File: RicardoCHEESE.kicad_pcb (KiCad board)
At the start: 4 copper layers, 138 parts, among them IC1 SiC437BED-T1-GE3, J0 Conn_01x05_Male, J1 Conn_01x05_Male, J10 USB_C_Receptacle_USB2.0, J101 RBUS, J2 Conn_01x05_Male, J3 Conn_01x05_Male, J4 Conn_Coaxial, J601 Conn_01x02_Male, U1 HEF4051BT, U101 ESP32-S3, U201 SN65HVD230, U3 RTC6705, U4 SE5005L, U401 LM66200DRLR, U402 MAX77827AEFD+T, U403 SC4215, Y101 40MHz±10ppm, Y3 8MHz

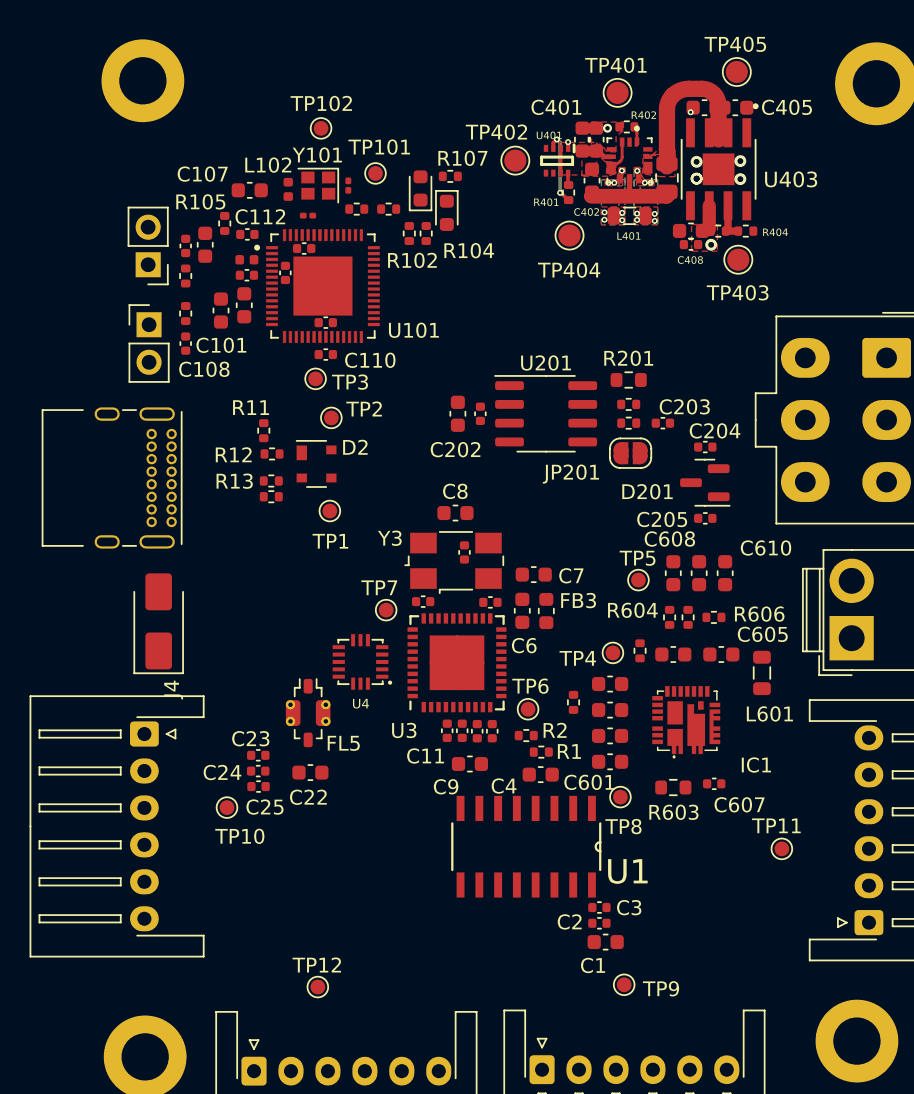
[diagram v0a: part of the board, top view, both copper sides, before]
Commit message: Add photo triggers
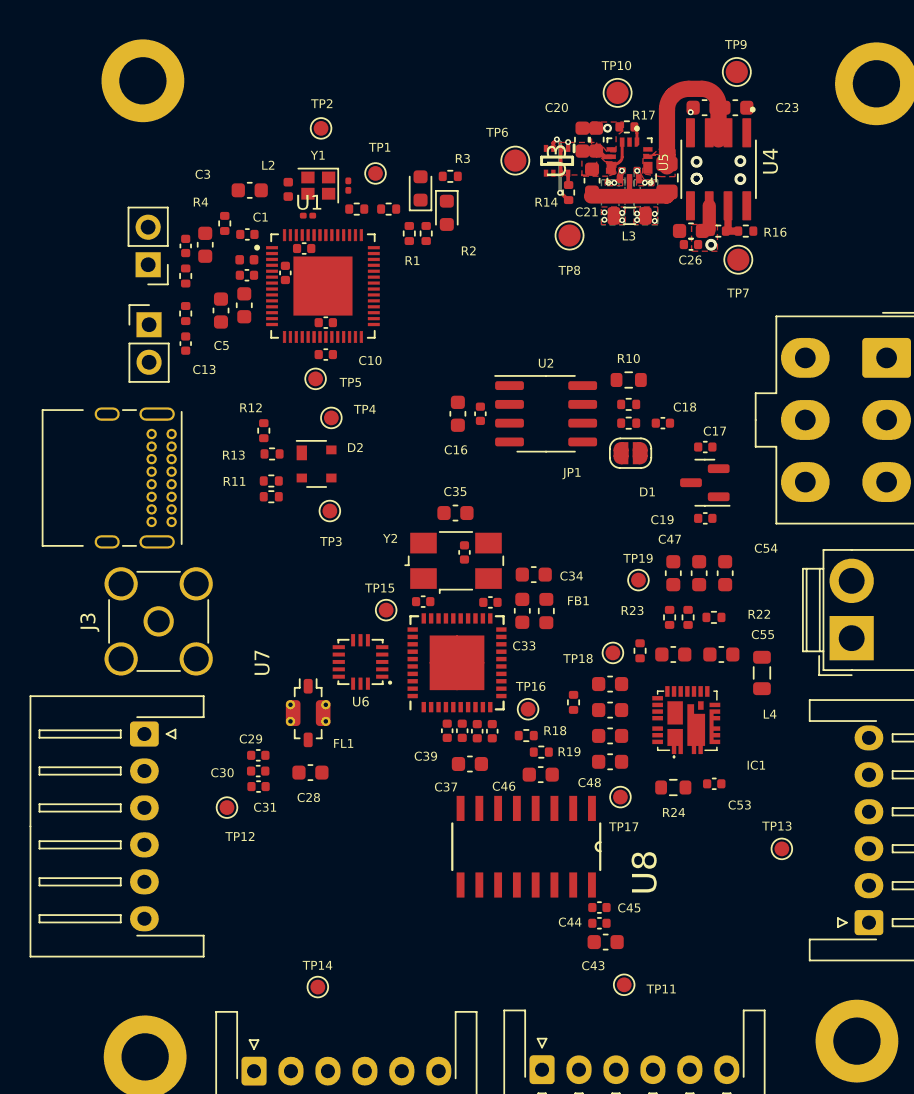
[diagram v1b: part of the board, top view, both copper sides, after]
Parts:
- J3: renamed from J4; footprint Diode_SMD:D_SMA -> Connector_Coaxial:SMA_Amphenol_901-144_Vertical
- U1: renamed from U101; footprint iclr:QFN40P700X700X90-57N -> fps:QFN40P700X700X90-57N
- U3: renamed from U401; footprint iclr:SOTFL50P160X60-8N -> fps:SOTFL50P160X60-8N
- U4: renamed from U403; footprint iclr:SOIC127P599X175-9N -> fps:SOIC127P599X175-8N
- U5: renamed from U402; footprint iclr:CONV_MAX77827AEFD+T -> fps:CONV_MAX77827AEFD+T
- U6: renamed from U4; footprint iclr:QFN300X300X100-16N -> fps:QFN300X300X100-16N
- U7: renamed from U3; footprint Custom:RTC6705 -> Ricardo-CHEESE:RTC6705
- U8: renamed from U1; footprint HEF4051BT:SOIC127P600X175-16N -> Ricardo-CHEESE:SOIC127P600X175-16N
- renumbered 12VLED101 to 12VLED1, 3V3LED101 to 3V3LED1, BOOTJUMPER101 to BOOTJUMPER1, C112 to C1, C110 to C10, C111 to C11, C103 to C12, C108 to C13, C102 to C14, C201 to C15, C202 to C16, C204 to C17, C203 to C18, C205 to C19, C113 to C2, C401 to C20, C402 to C21, C404 to C22, C405 to C23, C406 to C24, C407 to C25, C408 to C26, C403 to C27, C22 to C28, C23 to C29, C107 to C3, C24 to C30, C25 to C31, C5 to C32, C6 to C33, C7 to C34, C8 to C35, C14 to C36, C9 to C37, C10 to C38, C11 to C39, C109 to C4, C12 to C40, C13 to C41, C15 to C42, C1 to C43, C2 to C44, C3 to C45, C4 to C46, C608 to C47, C601 to C48, C602 to C49, C101 to C5, C603 to C50, C604 to C51, C609 to C52, C607 to C53, C610 to C54, C605 to C55, C606 to C56, C104 to C6, C105 to C7, C106 to C8, C114 to C9, D201 to D1, ENJUMPER101 to ENJUMPER1, FB3 to FB1, FL5 to FL1, H101 to H1, H102 to H2, H103 to H3, H104 to H4, J101 to J1, J10 to J2, J0 to J4, J1 to J5, J2 to J6, J3 to J7, J601 to J8, JP201 to JP1, L101 to L1, L102 to L2, L401 to L3, L601 to L4, R102 to R1, R201 to R10, R13 to R11, R11 to R12, R12 to R13, R401 to R14, R403 to R15, R404 to R16, R402 to R17, R2 to R18, R1 to R19, R104 to R2, R602 to R20, R605 to R21, R606 to R22, R604 to R23, R603 to R24, R601 to R25, R107 to R3, R105 to R4, R106 to R5, R101 to R6, R103 to R7, R202 to R8, R203 to R9, TP101 to TP1, TP401 to TP10, TP9 to TP11, TP10 to TP12, TP11 to TP13, TP12 to TP14, TP7 to TP15, TP6 to TP16, TP8 to TP17, TP4 to TP18, TP5 to TP19, TP102 to TP2, TP1 to TP3, TP2 to TP4, TP3 to TP5, TP402 to TP6, TP403 to TP7, TP404 to TP8, TP405 to TP9, TXLED101 to TXLED1, U201 to U2, Y101 to Y1, Y3 to Y2

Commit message: Fixed libraries and footprints
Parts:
- added R26: 1k, Resistor_SMD:R_0402_1005Metric, F.Cu at (209.7, 91.1)
- added R27: 1k, Resistor_SMD:R_0402_1005Metric, F.Cu at (209.7, 93.1)
- added R28: 1k, Resistor_SMD:R_0402_1005Metric, F.Cu at (209.7, 95.1)
- added R29: 1k, Resistor_SMD:R_0402_1005Metric, F.Cu at (209.7, 97.1)
- added R30: 1k, Resistor_SMD:R_0402_1005Metric, F.Cu at (209.7, 99.1)
- added R31: 1k, Resistor_SMD:R_0402_1005Metric, F.Cu at (212.6, 91.1)
- added R32: 1k, Resistor_SMD:R_0402_1005Metric, F.Cu at (212.6, 93.1)
- added R33: 1k, Resistor_SMD:R_0402_1005Metric, F.Cu at (212.6, 95.1)
- added R34: 1k, Resistor_SMD:R_0402_1005Metric, F.Cu at (212.6, 97.1)
- added R35: 1k, Resistor_SMD:R_0402_1005Metric, F.Cu at (212.6, 99.1)
- IC1: footprint SIC437BED-T1-GE3:SIC437BEDT1GE3 -> fps:SiC437BEDT1GE3
- J3: footprint Connector_Coaxial:SMA_Amphenol_901-144_Vertical -> Connector_Coaxial:SMA_Molex_73251-1153_EdgeMount_Horizontal
- J4, J5, J6, J7: value Conn_01x05_Male -> Conn_01x06_Pin; footprint Connector_JST:JST_XH_S6B-XH-A-1_1x06_P2.50mm_Horizontal -> Connector_JST:JST_PH_S6B-PH-K_1x06_P2.00mm_Horizontal
- moved J4 5.46 mm to (159.8, 127.6)
- moved J5 5.27 mm to (139.5, 112.2)
- moved J3 2.77 mm to (138.3, 102.3), turned to 0 degrees
- moved J7 2.52 mm to (144.3, 127.7)
- moved J6 2.26 mm to (184.8, 119.0)
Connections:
- J4 pad 1: 5V_PWR -> Net-(J4-Pin_1)
- J4 pad 4: CAMERA_PWR_DET -> Net-(J4-Pin_4)
- J4 pad 5: CAMERA0_TRIG -> Net-(J4-Pin_5)
- J4 pad 6: (no net) -> Net-(J4-Pin_6)
- J5 pad 1: 5V_PWR -> Net-(J4-Pin_1)
- J5 pad 4: CAMERA_PWR_DET -> Net-(J4-Pin_4)
- J5 pad 5: CAMERA1_TRIG -> Net-(J5-Pin_5)
- J5 pad 6: (no net) -> Net-(J5-Pin_6)
- J6 pad 1: 5V_PWR -> Net-(J4-Pin_1)
- J6 pad 4: CAMERA_PWR_DET -> Net-(J4-Pin_4)
- J6 pad 5: CAMERA2_TRIG -> Net-(J6-Pin_5)
- J6 pad 6: (no net) -> Net-(J6-Pin_6)
- J7 pad 1: 5V_PWR -> Net-(J4-Pin_1)
- J7 pad 4: CAMERA_PWR_DET -> Net-(J4-Pin_4)
- J7 pad 5: CAMERA3_TRIG -> Net-(J7-Pin_5)
- J7 pad 6: (no net) -> Net-(J7-Pin_6)
- U1 pad 16: CAMERA0_TRIG -> PHOTO0_TRIG
- U1 pad 17: CAMERA1_TRIG -> PHOTO1_TRIG
- U1 pad 18: CAMERA2_TRIG -> PHOTO2_TRIG
- U1 pad 19: CAMERA3_TRIG -> PHOTO3_TRIG
- U1 pad 38: unconnected-(U1-GPIO33-Pad38) -> CAMERA0_TRIG
- U1 pad 39: unconnected-(U1-GPIO34-Pad39) -> CAMERA1_TRIG
- U1 pad 40: unconnected-(U1-GPIO35-Pad40) -> CAMERA2_TRIG
- U1 pad 41: unconnected-(U1-GPIO36-Pad41) -> CAMERA3_TRIG
- U4 pad 5: (no net) -> unconnected-(U4-NC-Pad5)

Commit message: User saved
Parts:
- moved R31 76.4 mm to (142.8, 122.1)
- moved R30 70.2 mm to (142.8, 120.3)
- moved R34 66.2 mm to (152.4, 124.5), turned to 90 degrees
- moved R27 66.0 mm to (144.8, 81.1), turned to 90 degrees
- moved R35 63.5 mm to (154.4, 124.5), turned to 90 degrees
- moved R26 53.1 mm to (166.0, 121.3)
- moved R28 51.2 mm to (167.8, 124.5), turned to -90 degrees
- moved R29 48.4 mm to (169.8, 124.4), turned to 90 degrees
- moved R32 35.9 mm to (181.6, 111.1)
- moved R33 34.0 mm to (181.6, 109.1)
- moved TP11 7.11 mm to (172.0, 117.3)

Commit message: Placing footprints
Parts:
- moved C19 54.4 mm to (212.7, 52.7), turned to 90 degrees
- moved C16 52.3 mm to (208.1, 67.3), turned to 0 degrees
- moved JP1 51.0 mm to (210.3, 56.1), turned to 180 degrees
- moved D1 51.0 mm to (210.3, 52.7), turned to -90 degrees
- moved C15 50.9 mm to (207.5, 66.0), turned to 0 degrees
- moved U2 47.7 mm to (206.3, 61.7), turned to 90 degrees
- moved C17 47.6 mm to (207.9, 52.7), turned to 90 degrees
- moved C18 47.1 mm to (207.9, 54.7), turned to 90 degrees
- moved R9 46.7 mm to (207.0, 56.9), turned to -90 degrees
- moved R8 44.9 mm to (205.7, 56.9), turned to 90 degrees
- moved J1 43.8 mm to (203.9, 41.0), turned to 0 degrees
- moved C21 41.9 mm to (202.9, 93.1)
- moved C24 41.9 mm to (210.6, 88.1)
- moved C27 41.9 mm to (203.2, 90.3)
- moved R16 41.9 mm to (213.3, 96.5)
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
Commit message: Board layout
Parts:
- moved TP7 80.7 mm to (136.2, 73.2), turned to 180 degrees
- moved R16 79.3 mm to (136.9, 75.2), turned to 180 degrees
- moved C23 76.0 mm to (136.8, 84.0), turned to 180 degrees
- moved R15 75.6 mm to (138.9, 75.2), turned to 180 degrees
- moved TP9 74.1 mm to (138.7, 86.4), turned to 180 degrees
- moved U4 73.7 mm to (138.9, 79.4), turned to 90 degrees
- moved C25 72.4 mm to (140.9, 73.8), turned to 180 degrees
- moved C26 72.2 mm to (140.9, 75.2), turned to 180 degrees
- moved C16 72.2 mm to (135.8, 68.4), turned to -90 degrees
- moved C24 70.8 mm to (139.8, 84.0), turned to 0 degrees
- moved C15 70.4 mm to (137.2, 67.8), turned to -90 degrees
- moved C22 66.7 mm to (142.8, 78.9), turned to 90 degrees
- moved C19 65.5 mm to (150.4, 73.0), turned to 0 degrees
- moved U2 65.0 mm to (141.5, 66.6), turned to 0 degrees
- moved JP1 64.9 mm to (147.1, 70.6), turned to 90 degrees
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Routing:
- net /Power/BBOUT: track 12.3 -> 0.00 mm
- net GND: track 6.73 -> 0.00 mm, vias 8 -> 0
- net VBUS: track 5.27 -> 0.00 mm, vias 2 -> 0
- net /Power/FBIn: track 2.61 -> 0.00 mm
- net /Power/BBIN: track 2.00 -> 0.00 mm
- net /Power/VoutDiode: track 1.68 -> 0.00 mm
- net +3.3V: track 1.61 -> 0.00 mm, vias 1 -> 0
- net /Power/BIAS: track 1.42 -> 0.00 mm
- net /Power/SEL: track 1.01 -> 0.00 mm
- net Net-(U3-ST): track 0.81 -> 0.00 mm
- net /Power/LX2: vias 7 -> 0
- net /Power/LX1: vias 7 -> 0
- removed copper zone on F.Cu, net +3.3V
- removed copper zone on F.Cu, net /Power/BBIN
- removed copper zone on F.Cu, net /Power/BBOUT
- removed copper zone on B.Cu, net /Power/LX1
- removed copper zone on F.Cu, net /Power/LX1
- removed copper zone on B.Cu, net /Power/LX2
- removed copper zone on F.Cu, net /Power/LX2
- removed copper zone on F.Cu, net GND
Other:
- board outline added: 54.4 x 77.3 mm

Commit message: Some routing
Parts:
- moved J8 4.42 mm to (162.5, 95.8), turned to -90 degrees
- turned R28 to 90 degrees
- turned R32 to 180 degrees
- turned R33 to 180 degrees
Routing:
- net Net-(J4-Pin_4): track 0.00 -> 69.5 mm
- net /Camera System/CAMERA1: track 0.00 -> 27.1 mm
- net GND: track 0.00 -> 26.0 mm, vias 0 -> 8
- net +3.3V: track 0.00 -> 25.0 mm
- net /Camera System/CAMERA2: track 0.00 -> 21.0 mm
- net /Data+: track 0.00 -> 20.6 mm, vias 0 -> 1
- net /Camera System/CAMERA3: track 0.00 -> 19.1 mm
- net Net-(IC1-VIN_1): track 0.00 -> 18.7 mm
- net /Data-: track 0.00 -> 17.2 mm
- net /CAN+: track 0.00 -> 16.3 mm
- net /CAN-: track 0.00 -> 15.5 mm
- net RBUS_uC_V: track 0.00 -> 13.9 mm
- net Net-(IC1-SW_1): track 0.00 -> 13.3 mm
- net 5V_PWR: track 0.00 -> 12.8 mm
- net +3.3VA: track 0.00 -> 11.9 mm, vias 0 -> 2
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- added copper zone on In2.Cu, net GND

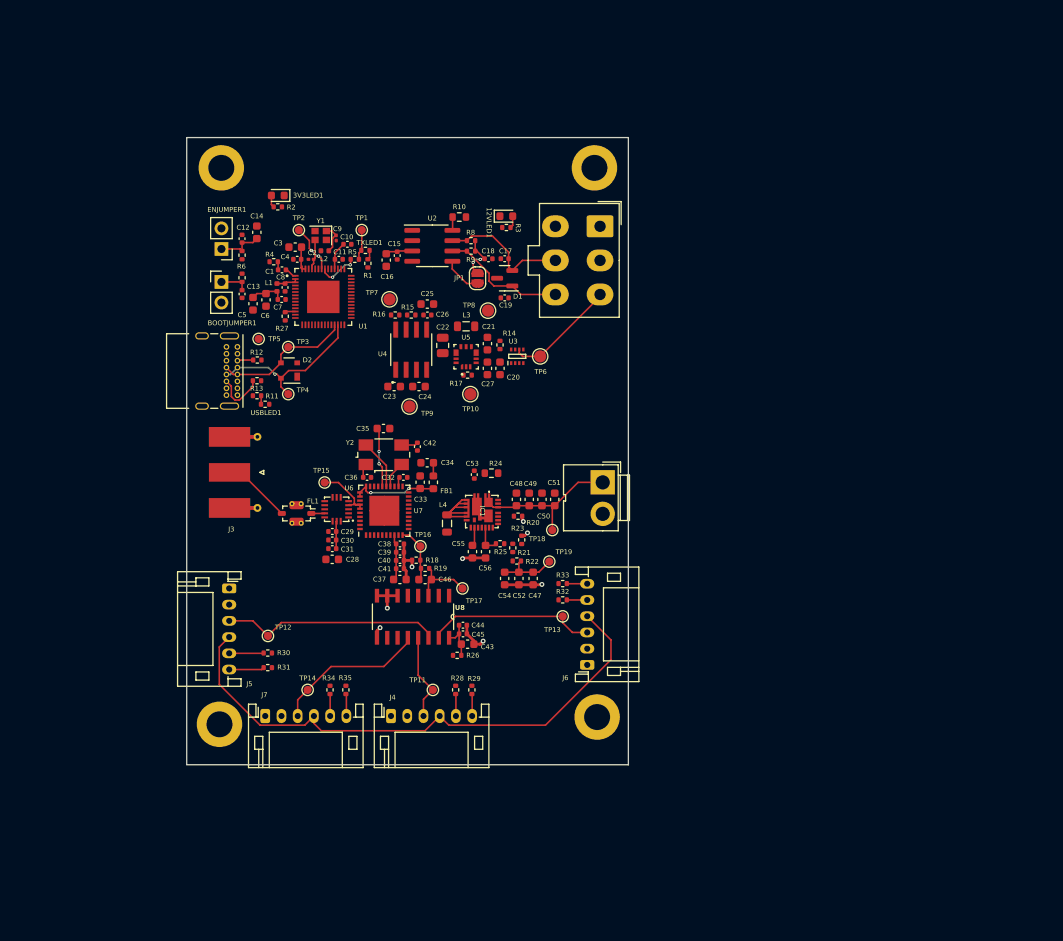
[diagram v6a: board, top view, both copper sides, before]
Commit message: Camera buck changes, c and r footprints, other
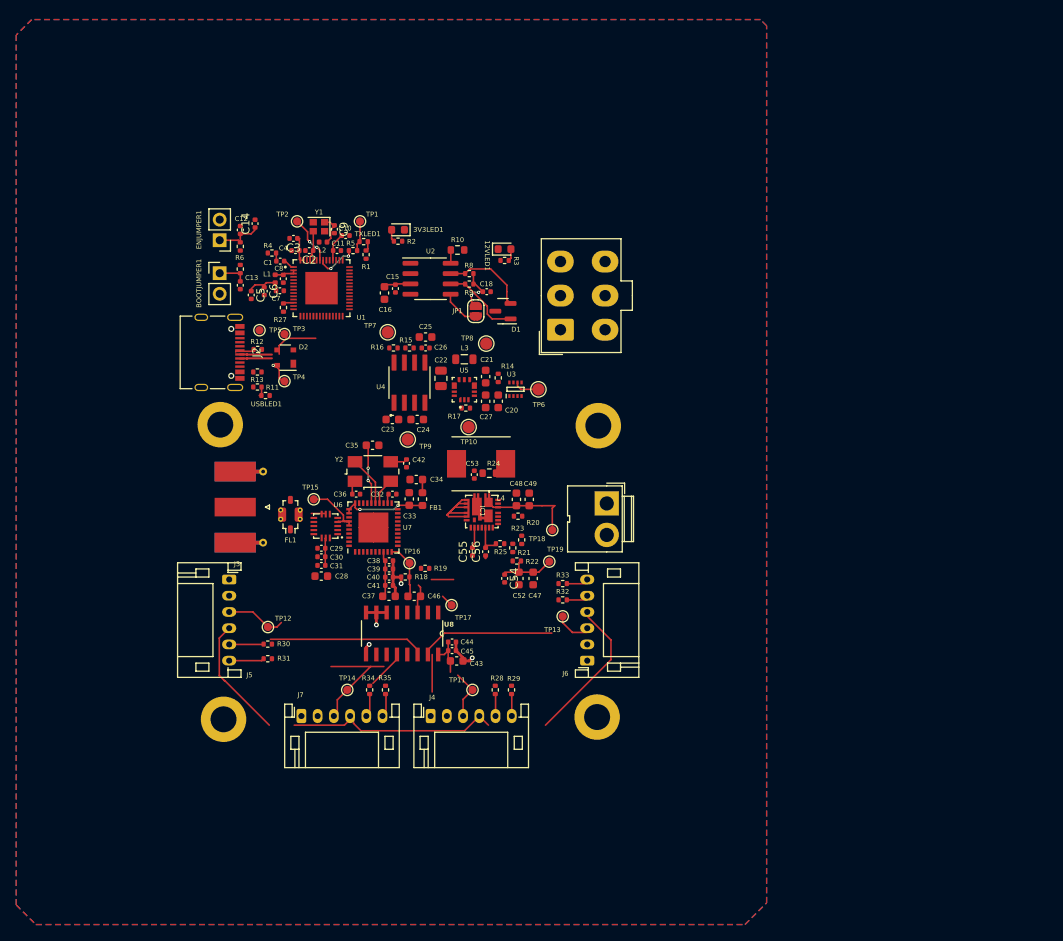
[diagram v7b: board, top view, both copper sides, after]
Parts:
- removed C17, C19: 220pF, Capacitor_SMD:C_0402_1005Metric
- removed C50, C51: 2u2, Capacitor_SMD:C_0603_1608Metric
- removed R26: 1k, Resistor_SMD:R_0402_1005Metric
- C14, C3, C5, C55, C56, C6: footprint Capacitor_SMD:C_0603_1608Metric -> Capacitor_SMD:C_0402_1005Metric
- C2, C9: footprint Capacitor_SMD:C_0201_0603Metric -> Capacitor_SMD:C_0402_1005Metric
- C49: value 2u2 -> 1u5
- C54: value 3u3 -> 100n; footprint Capacitor_SMD:C_0603_1608Metric -> Capacitor_SMD:C_0402_1005Metric
- J2: footprint Connector_USB:USB_C_Receptacle_GCT_USB4085 -> Connector_USB:USB_C_Receptacle_Palconn_UTC16-G
- L4: footprint Inductor_SMD:L_0805_2012Metric -> Ricardo-CHEESE:IND_ASPI-0630HI-6R8M-T15
- R25: value 51k -> 200k
- moved H2 31.8 mm to (161.9, 88.8)
- moved H1 31.6 mm to (115.4, 88.7)
- moved R2 15.4 mm to (137.3, 66.1)
- moved 3V3LED1 15.4 mm to (137.3, 64.7)
- moved J1 13.6 mm to (157.3, 77.0), turned to 90 degrees
- moved L4 8.47 mm to (147.5, 93.5), turned to 180 degrees
- moved J4 4.88 mm to (141.3, 124.6)
- moved R28 4.88 mm to (149.3, 121.3)
- moved R29 4.88 mm to (151.3, 121.3)
- moved R34 4.88 mm to (133.8, 121.3)
- moved R35 4.88 mm to (135.7, 121.3)
- moved TP11 4.88 mm to (146.4, 121.3)
- moved TP14 4.88 mm to (131.0, 121.3)
- moved J7 4.46 mm to (125.4, 124.6)
- moved J3 4.33 mm to (118.9, 98.8)
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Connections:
- C13 pad 1: /BOOT -> GND
- C13 pad 2: GND -> /BOOT
- C14 pad 1: /CHIP_PU -> GND
- C14 pad 2: GND -> /CHIP_PU
- C56 pad 1: GND -> /Camera System/Camera Power Buck Converter/GNDA
- D2 pad 2: +3.3V -> VBUS
- IC1 pad 16: GND -> /Camera System/Camera Power Buck Converter/GNDA
- IC1 pad 25: GND -> /Camera System/Camera Power Buck Converter/GNDA
- J2 pad A4: +3.3V -> VBUS
- J2 pad A9: +3.3V -> VBUS
- J2 pad B4: +3.3V -> VBUS
- J2 pad B9: +3.3V -> VBUS
- J4 pad 1: Net-(J4-Pin_1) -> 5V_PWR
- J5 pad 1: Net-(J4-Pin_1) -> 5V_PWR
- J6 pad 1: Net-(J4-Pin_1) -> 5V_PWR
- J7 pad 1: Net-(J4-Pin_1) -> 5V_PWR
- R11 pad 1: +3.3V -> VBUS
- R20 pad 2: GND -> /Camera System/Camera Power Buck Converter/GNDA
- R23 pad 2: GND -> /Camera System/Camera Power Buck Converter/GNDA
- R25 pad 1: Net-(IC1-VDD) -> /Camera System/Camera Power Buck Converter/GNDA
- TP5 pad 1: +3.3V -> VBUS
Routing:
- net /Data+: track 20.6 -> 7.22 mm
- net RBUS_uC_V: track 13.9 -> 3.18 mm
- net Net-(J4-Pin_4): track 69.5 -> 59.9 mm
- net Net-(FL1-OUT): track 8.54 -> 0.00 mm
- net /Data-: track 17.2 -> 9.88 mm
- net Net-(IC1-VIN_1): track 18.7 -> 11.6 mm
- net Net-(J2-CC2): track 6.36 -> 0.00 mm
- net GND: track 26.0 -> 20.0 mm, vias 8 -> 4
- net /CAN+: track 16.3 -> 10.4 mm
- net /CAN-: track 15.5 -> 9.73 mm
- net /Camera System/RFOUT: track 1.66 -> 0.02 mm
- added copper zone on In2.Cu, net +3.3V
- added copper zone on B.Cu, net GND
- added copper zone on F.Cu, net GND
- added copper zone on In1.Cu, net GND
- removed copper zone on In2.Cu, net GND
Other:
- board outline removed
